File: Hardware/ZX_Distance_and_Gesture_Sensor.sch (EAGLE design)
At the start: 42 parts, among them Q1 MMBT2222A, Q2 MOSFET-NCHANNEL2N7002PW

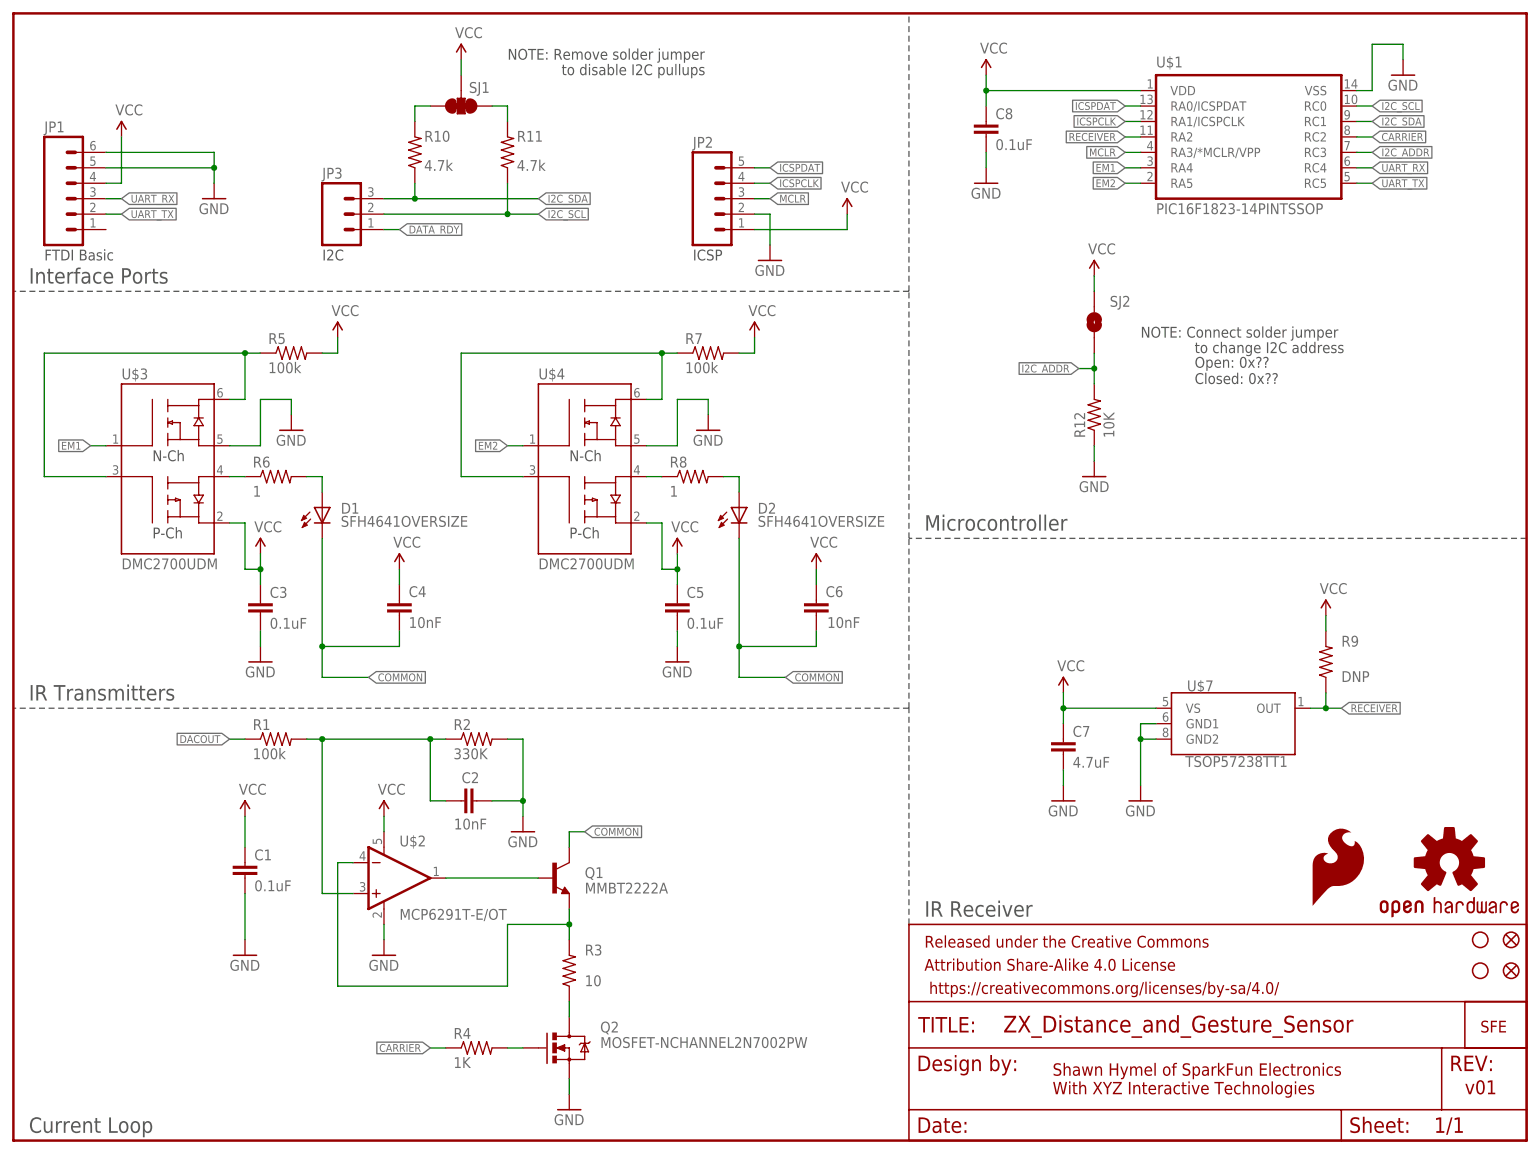
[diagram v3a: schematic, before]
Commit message: Completed layout. Ready for review before prototype.
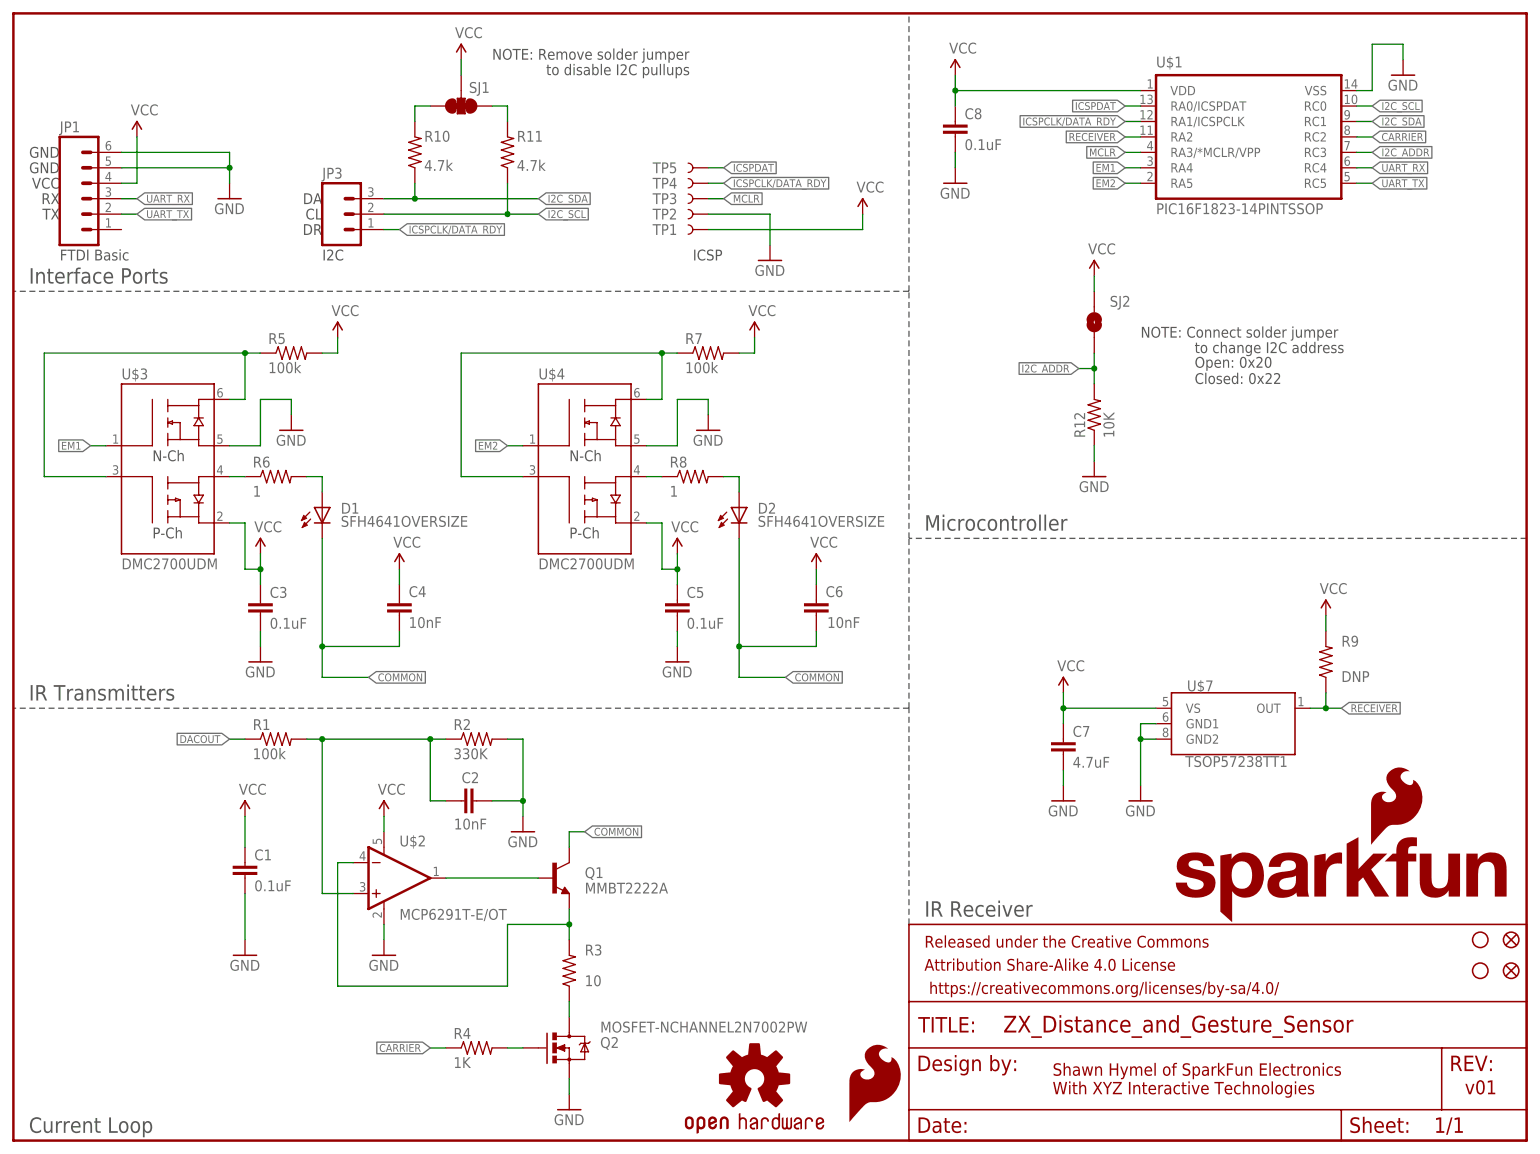
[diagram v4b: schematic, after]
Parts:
- removed JP2: (no value), SparkFun-Connectors:M05PTH
- added TP1, TP2, TP3, TP4, TP5: TEST-POINT3X5, SparkFun-Passives:TEST-POINT3X5
- U$5: value SFE_LOGO_NAME_WEB -> SFE_LOGO_NAME_FLAME.1_INCH; device SparkFun-Aesthetics:SFE_LOGO_NAME_WEB -> SparkFun-Aesthetics:SFE_LOGO_NAME_FLAME.1_INCH
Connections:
- removed net DATA_RDY: JP3.1
- removed net ICSPCLK: JP2.4, U$1.RA1/ICSPCLK
- new net ICSPCLK/DATA_RDY: JP3.1, TP4.1, U$1.RA1/ICSPCLK
- net GND: now also TP2.1; no longer JP2.2
- net ICSPDAT: now also TP5.1; no longer JP2.5
- net MCLR: now also TP3.1; no longer JP2.3
- net VCC: now also TP1.1; no longer JP2.1
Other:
- note added: "CL"
- note added: "DA"
- note added: "DR"
- note added: "GND"
- note added: "Open: 0x20 Closed: 0x22"
- note added: "RX"
- note added: "TX"
- note added: "VCC"
- note removed: "Open: 0x?? Closed: 0x??"
- moved on the sheet: C8, JP1

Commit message: Added trace to DACOUT line. Made test point programming pads smaller. Added extra via on GND plane to beef up current carrying capability.
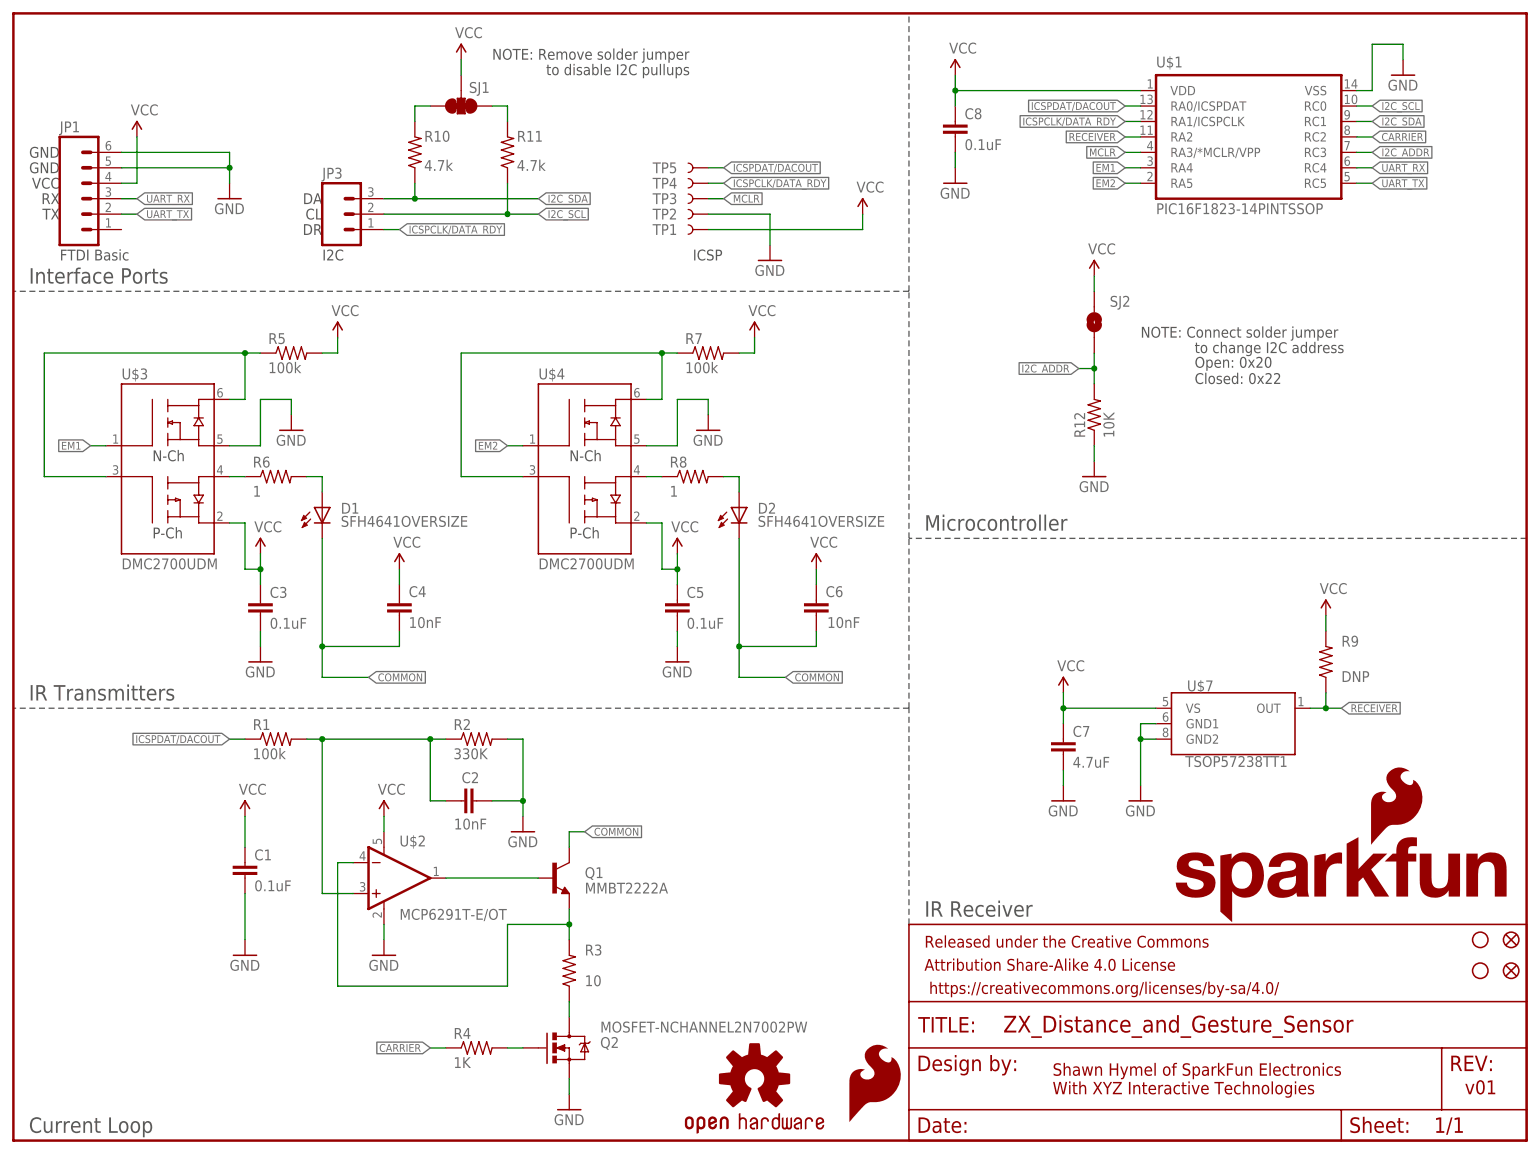
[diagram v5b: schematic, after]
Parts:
- TP1, TP2, TP3, TP4, TP5: value TEST-POINT3X5 -> TEST-POINT3X4; device SparkFun-Passives:TEST-POINT3X5 -> SparkFun-Passives:TEST-POINT3X4
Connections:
- removed net DACOUT: R1.1
- removed net ICSPDAT: TP5.1, U$1.RA0/ICSPDAT
- new net ICSPDAT/DACOUT: R1.1, TP5.1, U$1.RA0/ICSPDAT
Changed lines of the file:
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@@
 <setting verticaltext="up"/>
 </settings>
-<grid distance="0.1" unitdist="inch" unit="inch" style="lines" multiple="1" display="yes" altdistance="0.01" altunitdist="inch" altunit="inch"/>
+<grid distance="0.1" unitdist="inch" unit="inch" style="lines" multiple="1" display="no" altdistance="0.01" altunitdist="inch" altunit="inch"/>
 <layers>
 <layer number="1" name="Top" color="4" fill="1" visible="no" active="no"/>
@@
 <part name="STANDOFF1" library="SparkFun-Electromechanical" deviceset="STAND-OFF" device=""/>
 <part name="STANDOFF2" library="SparkFun-Electromechanical" deviceset="STAND-OFF" device=""/>
-<part name="TP1" library="SparkFun-Passives" deviceset="TEST-POINT" device="3X5"/>
-<part name="TP2" library="SparkFun-Passives" deviceset="TEST-POINT" device="3X5"/>
-<part name="TP3" library="SparkFun-Passives" deviceset="TEST-POINT" device="3X5"/>
-<part name="TP4" library="SparkFun-Passives" deviceset="TEST-POINT" device="3X5"/>
-<part name="TP5" library="SparkFun-Passives" deviceset="TEST-POINT" device="3X5"/>
+<part name="TP1" library="SparkFun-Passives" deviceset="TEST-POINT" device="3X4" value="TEST-POINT3X4"/>
+<part name="TP2" library="SparkFun-Passives" deviceset="TEST-POINT" device="3X4" value="TEST-POINT3X4"/>
+<part name="TP3" library="SparkFun-Passives" deviceset="TEST-POINT" device="3X4" value="TEST-POINT3X4"/>
+<part name="TP4" library="SparkFun-Passives" deviceset="TEST-POINT" device="3X4" value="TEST-POINT3X4"/>
+<part name="TP5" library="SparkFun-Passives" deviceset="TEST-POINT" device="3X4" value="TEST-POINT3X4"/>
 </parts>
 <sheets>
@@
 </segment>
 </net>
-<net name="ICSPDAT" class="0">
+<net name="ICSPDAT/DACOUT" class="0">
 <segment>
 <wire x1="114.3" y1="160.02" x2="116.84" y2="160.02" width="0.1524" layer="91"/>
@@
 <wire x1="185.42" y1="170.18" x2="182.88" y2="170.18" width="0.1524" layer="91"/>
 <label x="182.88" y="170.18" size="1.27" layer="95" rot="R180" xref="yes"/>
+</segment>
+<segment>
+<pinref part="R1" gate="G$1" pin="1"/>
+<wire x1="38.1" y1="66.04" x2="35.56" y2="66.04" width="0.1524" layer="91"/>
+<label x="35.56" y="66.04" size="1.27" layer="95" rot="R180" xref="yes"/>
 </segment>
 </net>
@@
 </segment>
 </net>
-<net name="DACOUT" class="0">
-<segment>
-<pinref part="R1" gate="G$1" pin="1"/>
-<wire x1="38.1" y1="66.04" x2="35.56" y2="66.04" width="0.1524" layer="91"/>
-<label x="35.56" y="66.04" size="1.27" layer="95" rot="R180" xref="yes"/>
-</segment>
-</net>

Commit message: Replaced SMD LEDs with PTH. Added PTH Recv'r. Ripped up traces.
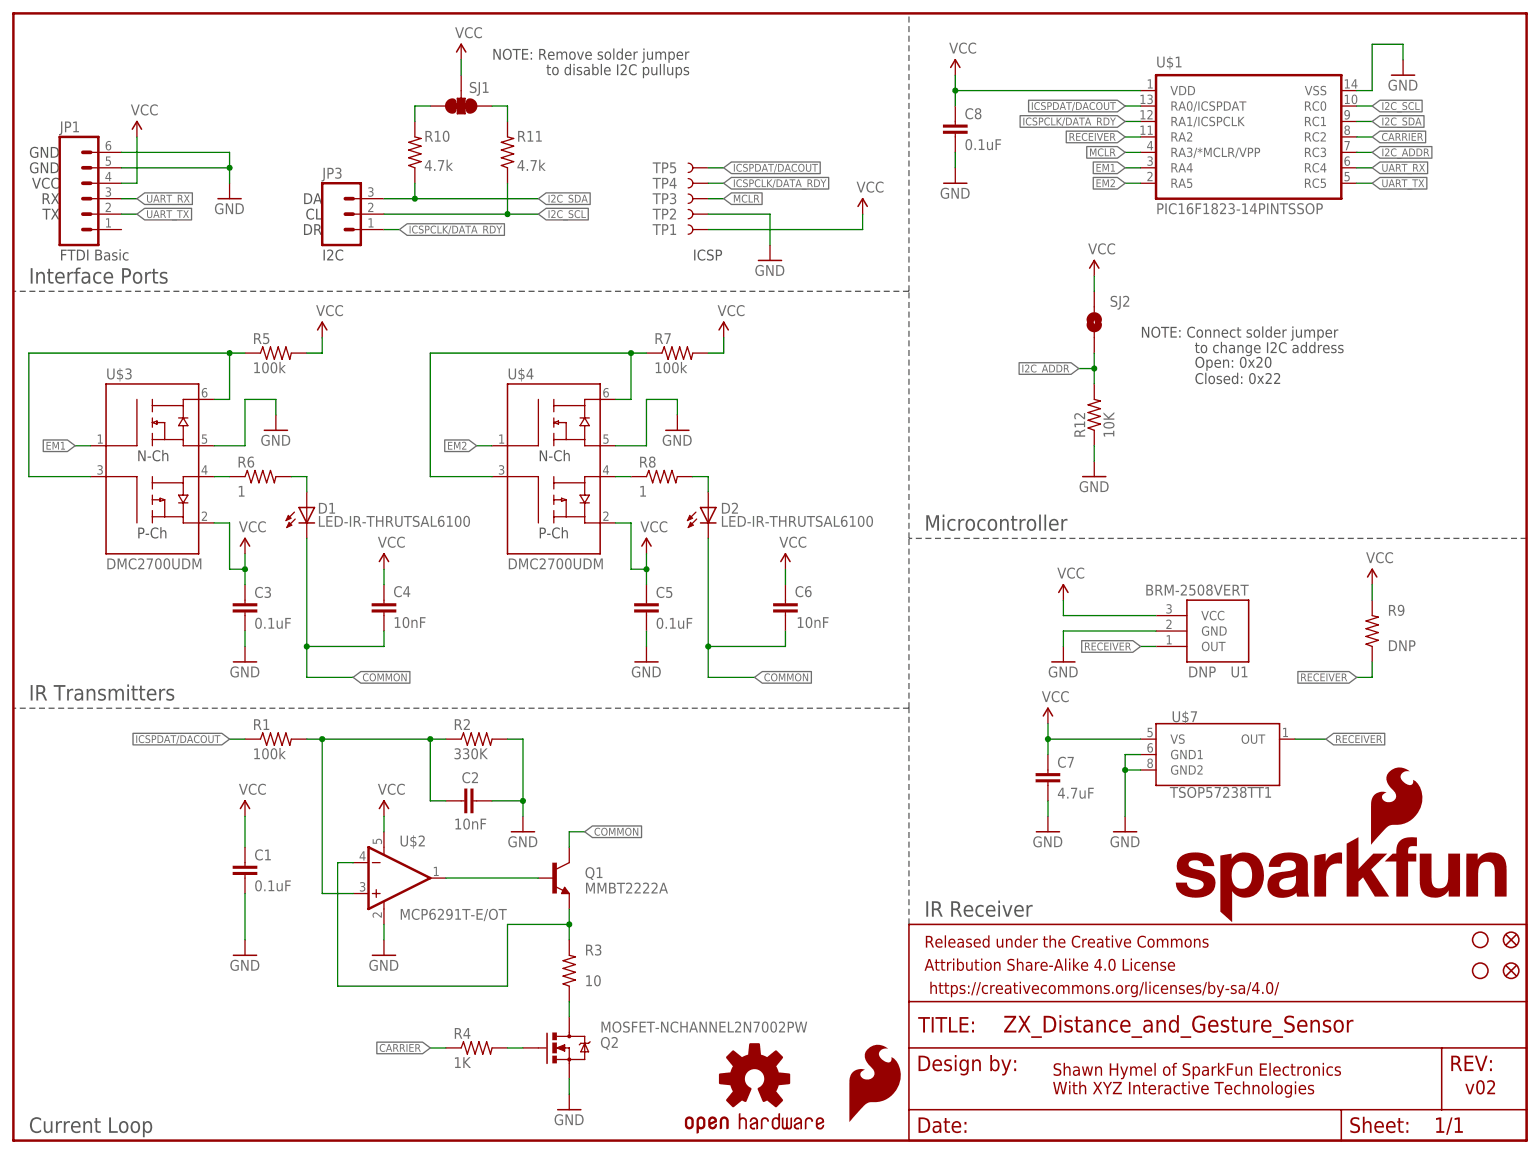
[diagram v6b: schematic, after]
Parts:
- added U1: BRM-2508VERT, SparkFun-Sensors:BRM-2508VERT
- D1, D2: value SFH4641OVERSIZE -> LED-IR-THRUTSAL6100; device SparkFun-LED:SFH4641OVERSIZE -> SparkFun-LED:LED-IR-THRUTSAL6100
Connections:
- net GND: now also U1.GND
- net RECEIVER: now also U1.OUT
- net VCC: now also U1.VCC
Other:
- note added: "v02"
- note removed: "v01"
- moved on the sheet: C3, C4, C5, C6, C7, D1, D2, R5, R6, R7, R8, R9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
